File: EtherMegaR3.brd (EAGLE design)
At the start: 101.6 x 53.3 mm, 115 parts, among them IC1 EUP3476SO08T, IC2 APX811-44UG-7, IC3 ATMEGA8U2-MU, IC6 W5100SQFP80, IC9 ATMEGA2560-16AU, J1 DC_2_1MM, P1 USB-FT, P3 ICSP:USB, P4 microSD, Q2 2N7002, Q3 2N7002, U1 HY931147C-RJ45, X1 16MHz, X2 25MHz, X3 16MHz

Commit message: Changes for R3 release
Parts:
- C6: value 47uF 25V -> 47uF 50V 1210 ceramic; device rcl:PANASONIC_D -> freetronics-jon:C1210
- IC3: value ATMEGA8U2-MU -> ATMEGA16U2-MU
- P1: value USB-FT -> USB-6PSMT; device freetronics-master-v1:USB-MINIB-FT -> freetronics-jon:USB-MICROB-MB05PMXX
- moved C6 39.3 mm to (59.4, 8.13), turned to 180 degrees
- moved L4 5.34 mm to (22.4, 4.83)
- moved C30 4.33 mm to (26.2, 47.6), turned to 180 degrees
- moved P1 3.05 mm to (1.52, 38.1), turned to 270 degrees
- moved SJ1 2.59 mm to (5.95, 43.1)
- moved C2 0.76 mm to (22.0, 42.4), turned to 270 degrees
- moved X1 0.51 mm to (18.5, 42.8)
- moved C12 0.51 mm to (22.0, 45.2)
- moved C8 0.51 mm to (22.0, 39.6)
- moved D1 0.25 mm to (15.7, 10.5)
- turned C37 to 0 degrees
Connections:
- removed net N$9: L3.1, P1.SH1, P1.SH2, P1.SH3, P1.SH4, Z1.2, Z2.2
- new net N$18: L3.1, P1.FIX1, P1.FIX2, P1.PIN1, P1.PIN2, P1.TAB1, P1.TAB2, Z1.2, Z2.2
- new net NC: JP6.8
- net 5V: now also C6.2, JP6.7; no longer C6.+
- net GND: now also C6.1; no longer C6.-
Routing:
- net SDA: track 37.6 -> 108.9 mm, vias 2 -> 3
- net N$9: track 38.7 -> 0.00 mm
- net N$18: track 0.00 -> 30.1 mm
- net SCL: track 81.5 -> 107.9 mm, vias 2 -> 3
- net VIN: track 68.3 -> 72.8 mm
- net 5V_PSU: track 67.6 -> 70.9 mm
- net N$16: track 5.97 -> 9.06 mm
- net N$74: track 18.6 -> 15.6 mm
- net N$113: track 10.8 -> 13.6 mm
- net N$17: track 6.47 -> 8.89 mm
- net AREF: track 76.6 -> 74.2 mm
- net N$70: track 21.8 -> 24.1 mm
- net RESET2: track 37.5 -> 39.5 mm
- net GND: track 138.1 -> 136.2 mm
- net D5: track 32.3 -> 31.1 mm
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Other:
- board text added: "2560 R3"
- board text added: "IO"
- board text added: "v2.0"
- board text removed: "2560"
- board text removed: "v1.1"

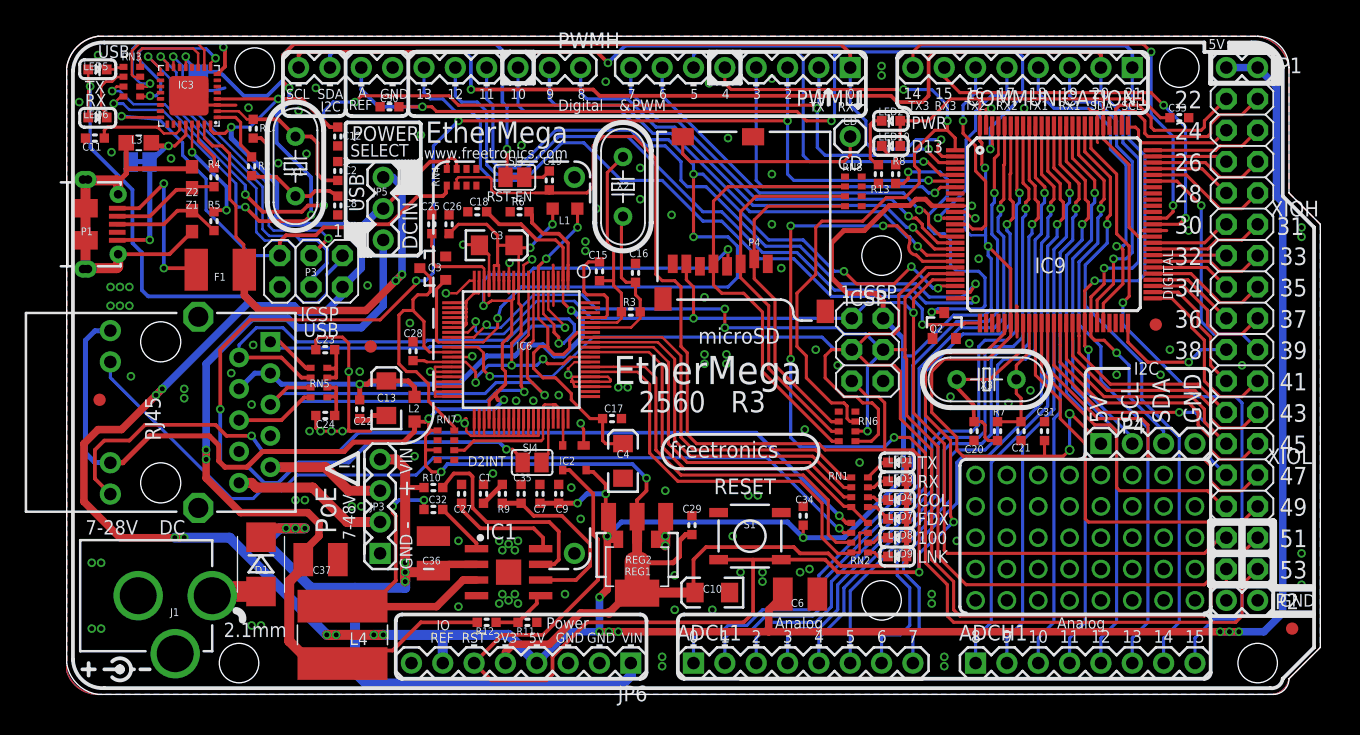
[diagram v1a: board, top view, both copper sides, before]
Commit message: Added MAC address chip and changed to hinge SD socket for v3.0 release
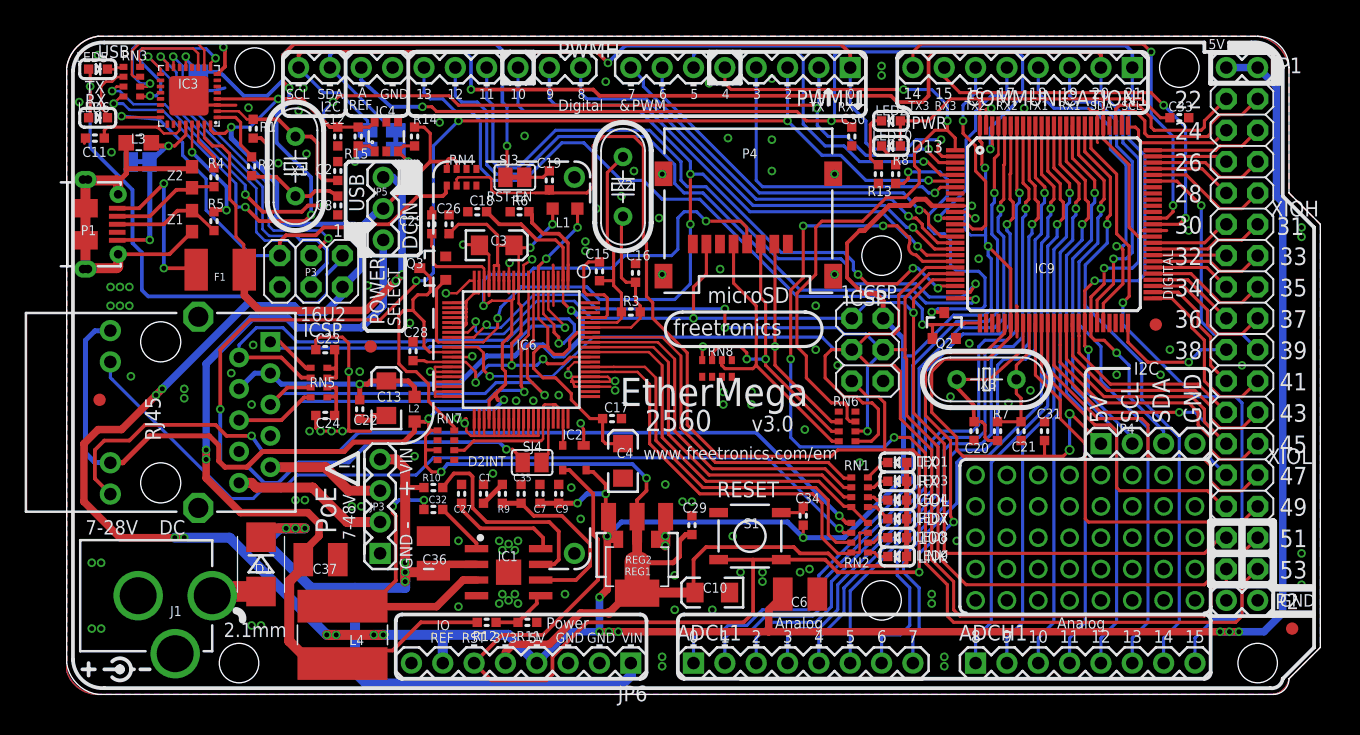
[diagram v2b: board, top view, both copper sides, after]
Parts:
- removed CD: M01PTH, freetronics-2:1X01
- added IC4: MCP24AA025E48, freetronics-jon:SOT23-6
- added R14, R15: 4K7, freetronics-master-v1.1:0603
- added SJ5, SJ6: (no value), freetronics-jon:SJC
- LED1, LED10, LED2, LED3, LED4, LED5, LED6, LED7, LED8, LED9: device freetronics:LED-0603 -> freetronics-jon:LED-0603
- P4: device freetronics-master-v1:MICRO-SD-SOCKET-PP -> freetronics-jon:MOLEX-SD-500901-003
- moved C30 37.5 mm to (63.6, 45.2), turned to 270 degrees
- moved RN8 18.1 mm to (52.7, 26.4), turned to 0 degrees
- moved P4 7.37 mm to (55.2, 45.8)
- moved LED5 0.05 mm to (2.54, 50.7), turned to 0 degrees
- turned LED6 to 0 degrees
- turned LED1 to 180 degrees
- turned LED10 to 180 degrees
- turned LED2 to 180 degrees
- turned LED3 to 180 degrees
- turned LED4 to 180 degrees
- turned LED7 to 180 degrees
- turned LED8 to 180 degrees
- turned LED9 to 180 degrees
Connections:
- removed net N$23: CD.1, P4.CD1
- new net N$19: IC4.3, R14.2, SJ5.2
- new net N$9: IC4.1, R15.2, SJ6.2
- net 5V: now also IC4.6, R14.1, R15.1
- net GND: now also IC4.2, IC4.4, IC4.5, P4.GND3, P4.GND4; no longer P4.CD2
- net SCL: now also SJ6.1
- net SDA: now also SJ5.1
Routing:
- net N$23: track 17.0 -> 0.00 mm
- net N$20: track 36.2 -> 23.3 mm
- net SCL: track 107.9 -> 116.1 mm
- net SDA: track 108.9 -> 116.4 mm
- net N$25: track 30.4 -> 24.0 mm, vias 0 -> 2
- net D10: track 90.4 -> 85.0 mm
- net 3V3D: track 189.5 -> 194.2 mm
- net 5V: track 472.7 -> 477.1 mm
- net N$9: track 0.00 -> 4.33 mm, vias 0 -> 1
- net N$19: track 0.00 -> 4.13 mm, vias 0 -> 1
- net N$24: track 27.4 -> 23.9 mm, vias 0 -> 2
- net D2: track 119.2 -> 116.7 mm
- net GND: track 136.2 -> 138.7 mm, vias 136 -> 139
- net D50_MISO: track 95.0 -> 96.8 mm
- net D5: track 31.1 -> 29.6 mm
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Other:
- board text added: "16U2"
- board text added: "2560"
- board text added: "EM"
- board text added: "I2C ADDR: 70 (0x50)"
- board text added: "ISOLATE MCP I2C"
- board text added: "K"
- board text added: "MCP 24AA025E48"
- board text added: "v3.0"
- board text added: "www.freetronics.com/em"
- board text removed: "CD"
- board text removed: "ETHERMEGA"
- board text removed: "v2.0"
- board text removed: "www.freetronics.com"
- board text removed: "www.freetronics.com/ethermega"

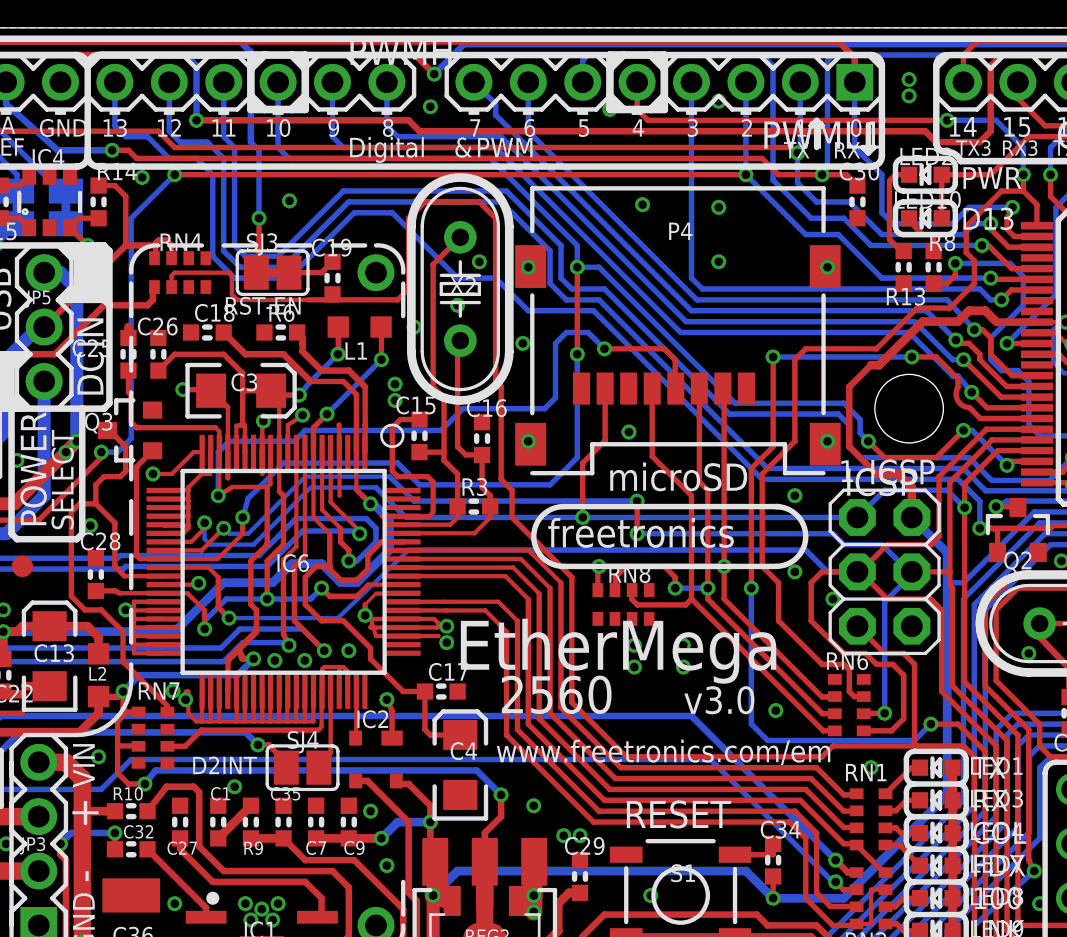
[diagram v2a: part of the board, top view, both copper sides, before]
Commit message: Added M02 header in parallel with RST-EN cut-track link for external reset mode control
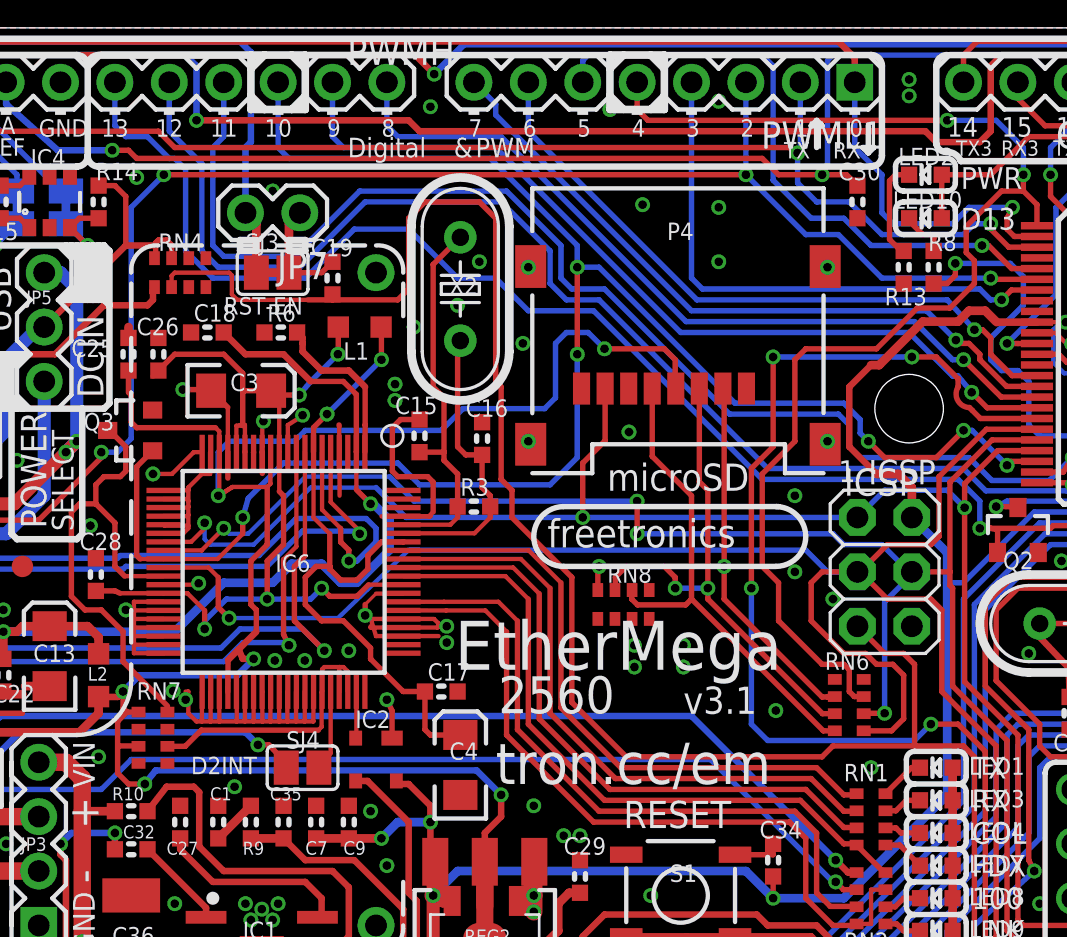
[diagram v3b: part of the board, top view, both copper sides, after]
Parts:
- added JP7: (no value), freetronics-master-v1.1:1X02
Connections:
- net DTR: now also JP7.2
- net N$75: now also JP7.1
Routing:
- net N$75: track 3.51 -> 6.52 mm
- net D11: track 58.0 -> 59.0 mm
- net D13: track 61.8 -> 61.2 mm
- net DTR: track 41.6 -> 41.9 mm, vias 2 -> 1
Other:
- board text added: "tron.cc/em"
- board text added: "v3.1"
